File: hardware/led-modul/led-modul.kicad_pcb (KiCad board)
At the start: 4 copper layers, 68 x 86.5 mm, 174 parts, among them J1 DEBUG, J2 BUS_IN, J201 24V IN 15A, J202 BLOKK 1, J203 BLOKK 2, J204 BLOKK 3, J3 BUS_OUT, J4 BŐVÍTŐ, Q201 NCEP6090AGU, Q202 NCE6080K, Q203 NCE6080K, Q204 NCE6080K, Q205 NCE6080K, Q206 NCE6080K, Q207 NCE6080K, U2 SN65HVD230D, U201 UCC27524DR, U202 UCC27524DR, U203 UCC27524DR, U205 MC78L12ACDR2G, U206 INA181A2IDBVR, U207 MCP9701AT-E/TT, U3 ESD2CAN24-Q1, U5 AP2112K-3.3TRG1, U6 STM32L433RCT3, Y1 8MHz

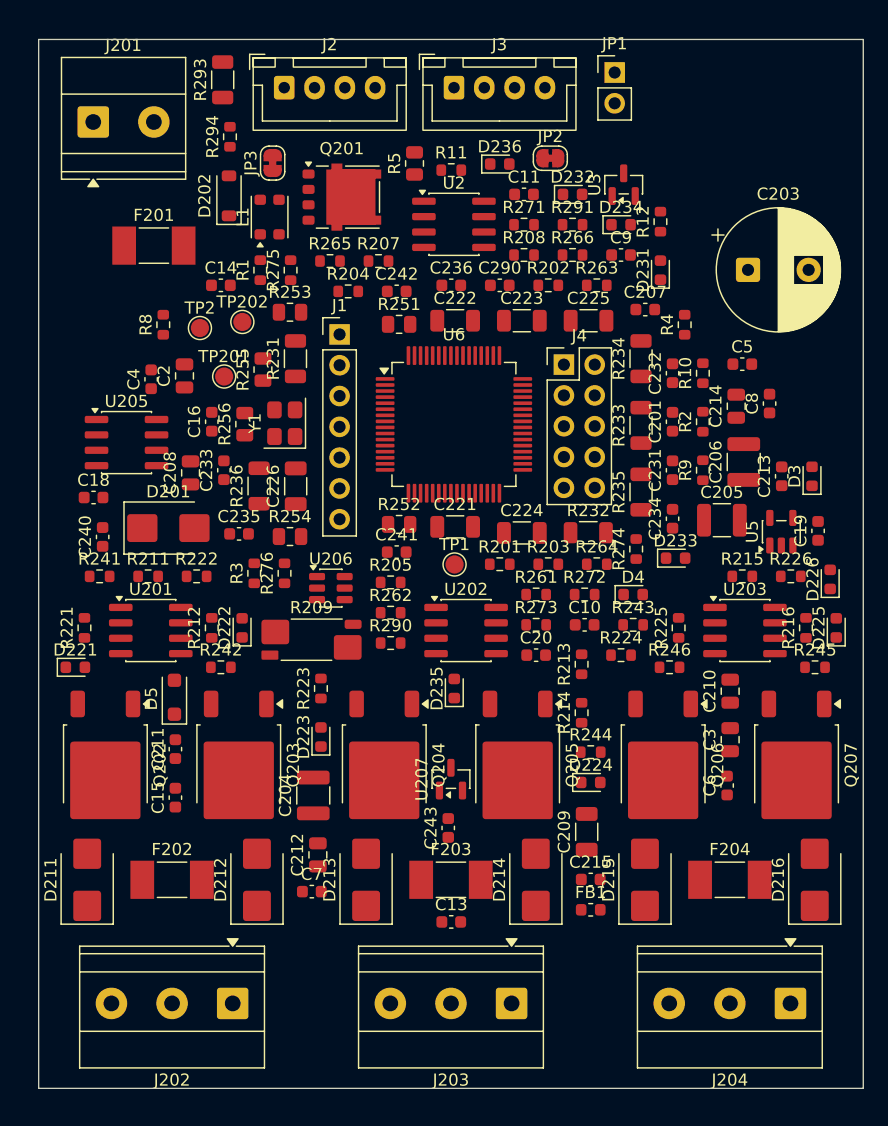
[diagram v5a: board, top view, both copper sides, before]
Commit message: Hardver: layout-előkészítés (D86) – JLC-szabályok és via-méretek, modulmag-blokk, a modulok elrendezése
- laponként .kicad_dru: JLC 4 réteg / 1 oz; via 0,3/0,45 (jel), 0,4/0,7 (táp), 0,6/1,0 mm (15 A); 230 V ↔ SELV 8 mm
- modulmag-blokk mindhárom modulon azonos relatív elrendezéssel (átvihető layout), 0,25 mm-es rács
- a sorkapcsok a Gainta D4MG fedélfurataira igazítva (5,08 mm), a kötött helyű alkatrészek zárolva
- LED-modul: LED-sor, meghajtók, FET-sor; relé: betáp és LED-sor; bemeneti: csatornánkénti oszlopok, ESD-sor
- lábhoz rendelés: hidegítők a tápjukhoz, gate-ellenállások a gate-hez; a vezérlő elrendezése még hátra (U4)
- docs/d4mg.pdf: a ház rajza; ellenorzes.py: 0 hiba

Co-Authored-By: Claude Opus 5.5 <noreply@anthropic.com>
Claude-Session: https://claude.ai/code/session_01KVtZMUPbtveTXy9VyJshyt
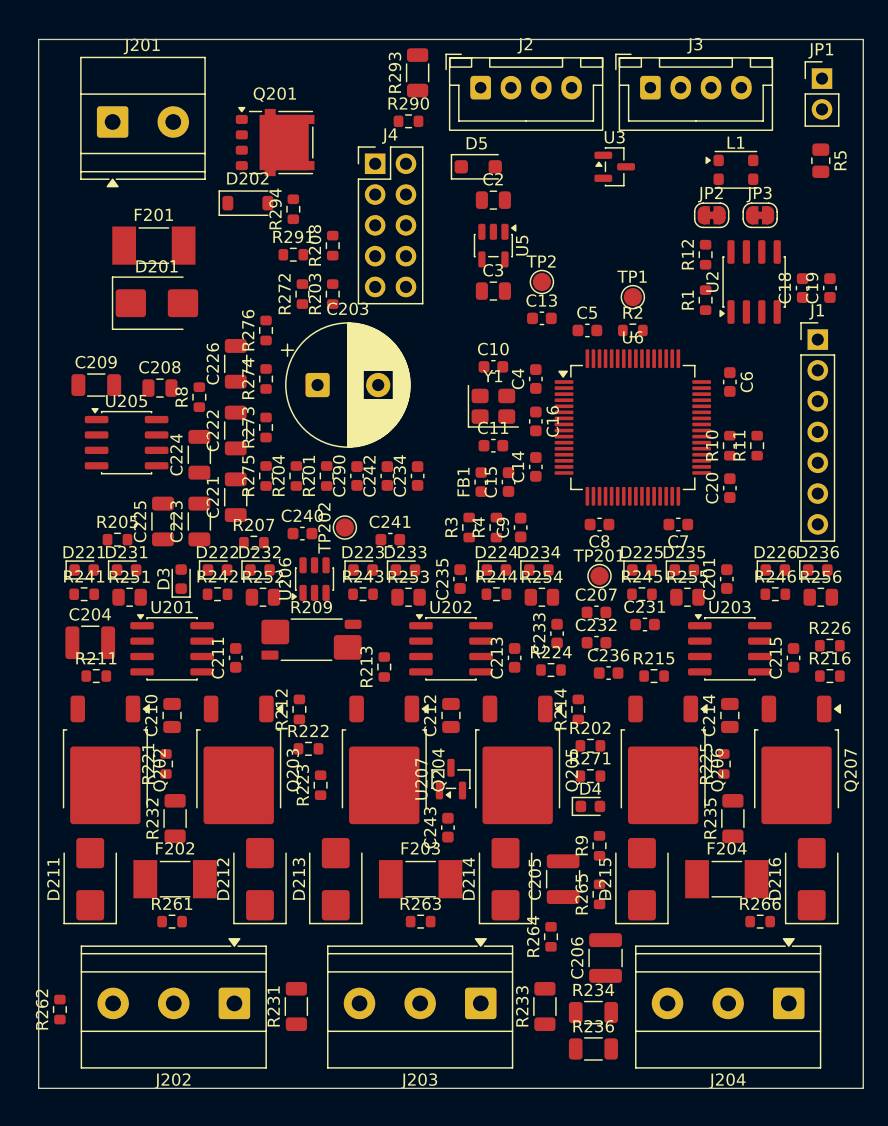
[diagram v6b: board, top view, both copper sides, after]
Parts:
- moved C18 61.0 mm to (163.0, 120.5), turned to 90 degrees
- moved R266 57.1 mm to (159.5, 172.8)
- moved R265 56.8 mm to (146.2, 170.5), turned to 90 degrees
- moved C209 54.7 mm to (104.8, 128.5), turned to 0 degrees
- moved R263 54.4 mm to (131.5, 172.8)
- moved R234 54.1 mm to (145.8, 180.2), turned to 0 degrees
- moved R236 54.0 mm to (145.8, 183.2), turned to 0 degrees
- moved R231 53.4 mm to (121.2, 179.8)
- moved D3 52.7 mm to (111.8, 144.5)
- moved D231 50.5 mm to (107.2, 143.8), turned to 0 degrees
- moved D5 50.4 mm to (136.2, 110.5), turned to 0 degrees
- moved C13 50.3 mm to (141.5, 123.0)
- moved R256 49.6 mm to (164.5, 146.0), turned to 0 degrees
- moved R233 48.6 mm to (141.8, 179.8)
- moved C210 46.1 mm to (111.0, 155.8)
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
